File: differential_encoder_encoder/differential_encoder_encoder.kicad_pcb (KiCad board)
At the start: 2 copper layers, 62.5 x 46.2 mm, 15 parts, among them J101 RJ45_LED_Shielded, J102 Conn_02x08_Odd_Even, U101 MAX489E, U102 MAX489E, U103 MAX489E

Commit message: tentative odrive positioning
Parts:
- J101: footprint Connector_RJ:RJ45_Wuerth_7499010121A_Horizontal -> Connector_RJ:RJ45_Amphenol_RJHSE538X
- U101, U102, U103: footprint Package_SO:SO-16_3.9x9.9mm_P1.27mm -> Package_SO:SO-14_3.9x8.65mm_P1.27mm
- moved J101 8.12 mm to (150.1, 69.3), turned to 90 degrees
- moved U103 2.47 mm to (178.1, 80.0)
- moved U101 2.43 mm to (178.1, 50.1)
- moved U102 2.41 mm to (178.1, 64.5)
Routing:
- net +5V: track 184.5 -> 220.0 mm
- net i+: track 24.9 -> 42.2 mm, vias 1 -> 3
- net b-: track 21.9 -> 39.1 mm, vias 1 -> 3
- net A: track 72.0 -> 82.3 mm, vias 1 -> 2
- net a+: track 23.3 -> 31.5 mm
- net I: track 49.2 -> 56.6 mm
- net Net-(J101-Pad12): track 2.71 -> 10.0 mm
- net Net-(U102-DE): track 3.85 -> 11.0 mm
- net Net-(J101-Pad10): track 3.21 -> 9.67 mm
- net GND: track 22.0 -> 16.5 mm, vias 8 -> 7
- net b+: track 21.3 -> 25.5 mm
- net Net-(U103-DE): track 4.28 -> 8.31 mm
- net a-: track 27.9 -> 30.5 mm
- net B: track 24.9 -> 27.2 mm
- net Net-(U101-DE): track 4.06 -> 5.91 mm
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
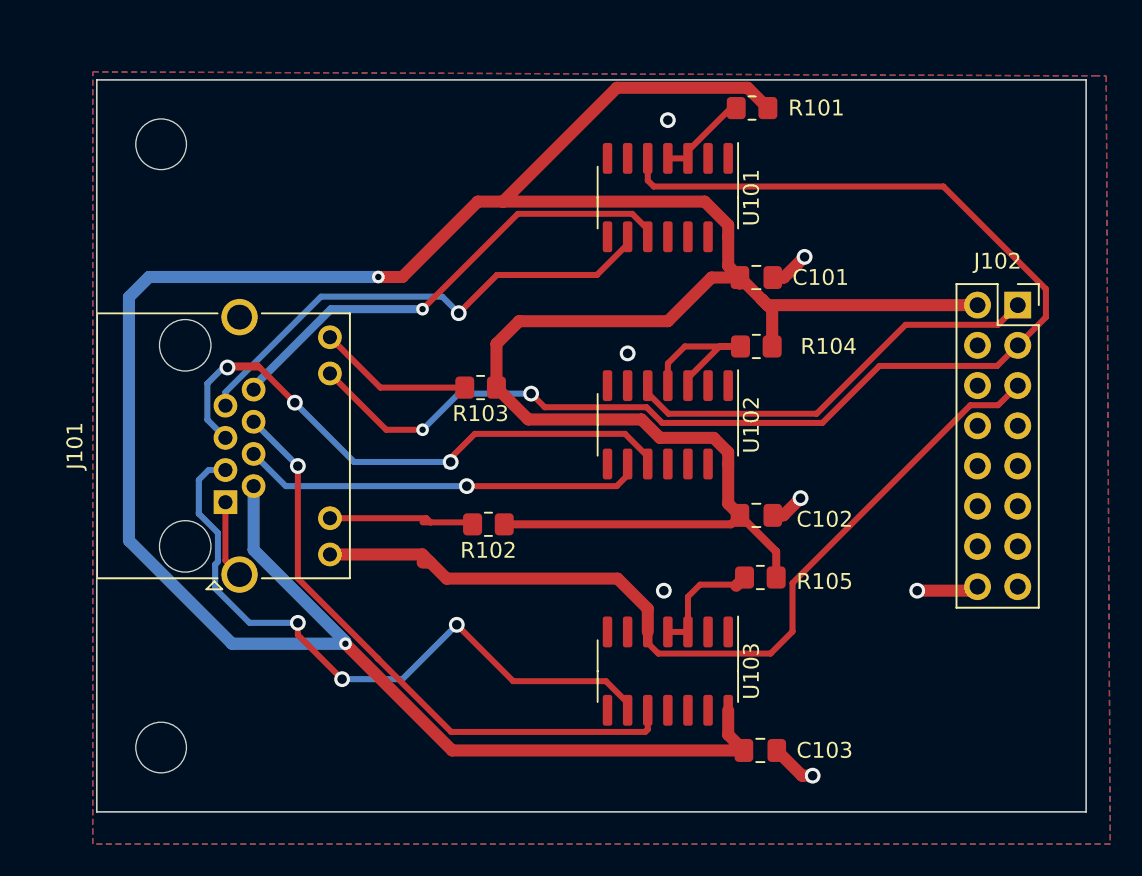
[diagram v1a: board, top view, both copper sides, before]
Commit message: new encoder layout
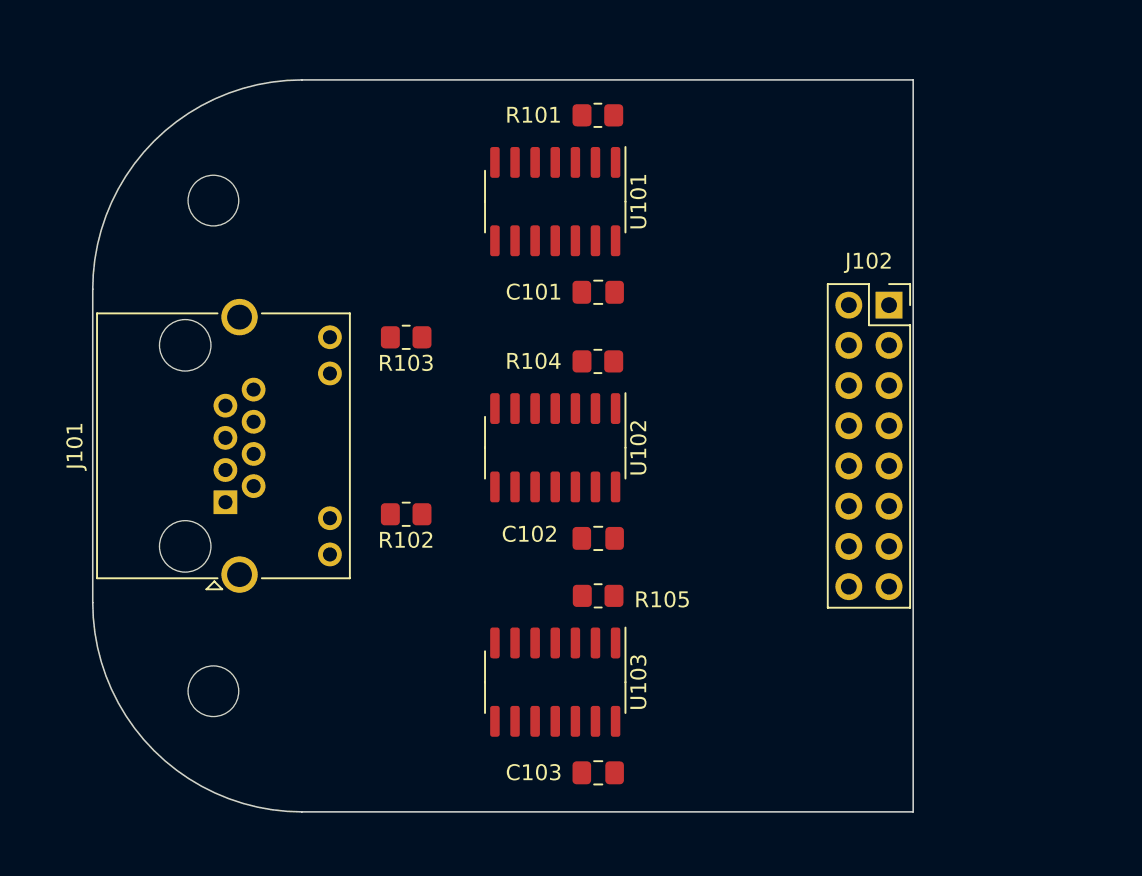
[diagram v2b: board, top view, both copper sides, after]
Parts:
- R105: value 100 -> locked
- moved C103 10.3 mm to (173.7, 86.4), turned to 180 degrees
- moved R105 10.3 mm to (173.7, 75.3)
- moved C102 10.1 mm to (173.7, 71.6), turned to 180 degrees
- moved R104 10.1 mm to (173.6, 60.5)
- moved C101 10.0 mm to (173.7, 56.1), turned to 180 degrees
- moved R101 9.75 mm to (173.6, 44.9)
- moved J102 8.13 mm to (192.0, 56.9)
- moved U102 7.26 mm to (170.9, 65.9)
- moved U103 7.15 mm to (170.9, 80.7)
- moved U101 7.12 mm to (170.9, 50.4)
- moved R103 5.67 mm to (161.5, 58.9)
- moved R102 5.23 mm to (161.5, 70.1)
- moved REF** 4.85 mm to (149.4, 50.3)
- moved REF** 4.85 mm to (149.4, 81.3), turned to 90 degrees
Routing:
- net +5V: track 220.0 -> 0.00 mm, vias 2 -> 0
- net A: track 82.3 -> 0.00 mm, vias 2 -> 0
- net I: track 56.6 -> 0.00 mm
- net i+: track 42.2 -> 0.00 mm, vias 3 -> 0
- net b-: track 39.1 -> 0.00 mm, vias 3 -> 0
- net i-: track 38.5 -> 0.00 mm, vias 1 -> 0
- net a+: track 31.5 -> 0.00 mm, vias 1 -> 0
- net a-: track 30.5 -> 0.00 mm, vias 1 -> 0
- net B: track 27.2 -> 0.00 mm
- net b+: track 25.5 -> 0.00 mm, vias 1 -> 0
- net GND: track 16.5 -> 0.00 mm, vias 7 -> 0
- net Net-(U102-DE): track 11.0 -> 0.00 mm
- net Net-(J101-Pad12): track 10.0 -> 0.00 mm
- net Net-(J101-Pad10): track 9.67 -> 0.00 mm
- net Net-(U103-DE): track 8.31 -> 0.00 mm
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- removed copper zone on B.Cu, net GND
- removed copper zone on F.Cu, net GND
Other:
- board size 62.5 x 46.2 mm -> 51.8 x 46.2 mm

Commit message: encoder traces are now chonkers
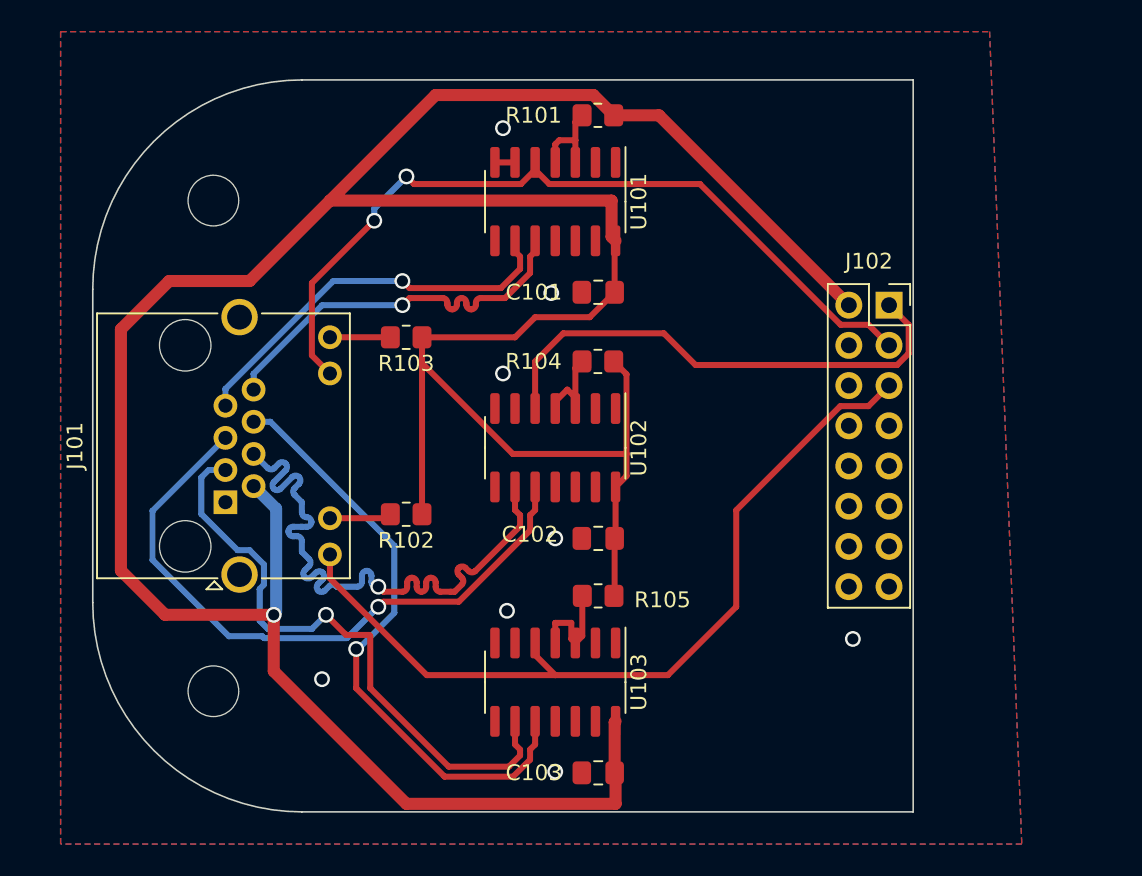
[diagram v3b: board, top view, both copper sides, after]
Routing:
- net +5V: track 0.00 -> 206.9 mm, vias 0 -> 1
- net I: track 0.00 -> 53.1 mm
- net A: track 0.00 -> 51.5 mm, vias 0 -> 2
- net b-: track 0.00 -> 41.2 mm, vias 0 -> 1
- net b+: track 0.00 -> 40.7 mm, vias 0 -> 1
- net i-: track 0.00 -> 38.5 mm, vias 0 -> 1
- net i+: track 0.00 -> 38.5 mm, vias 0 -> 1
- net B: track 0.00 -> 32.0 mm
- net a+: track 0.00 -> 25.1 mm, vias 0 -> 1
- net a-: track 0.00 -> 25.0 mm, vias 0 -> 1
- net Net-(U103-DE): track 0.00 -> 6.82 mm
- net Net-(U102-DE): track 0.00 -> 6.07 mm
- net Net-(U101-DE): track 0.00 -> 5.67 mm
- net Net-(J101-Pad10): track 0.00 -> 3.92 mm
- net Net-(J101-Pad12): track 0.00 -> 3.82 mm
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- added copper zone on B.Cu, net GND
- added copper zone on F.Cu, net GND
